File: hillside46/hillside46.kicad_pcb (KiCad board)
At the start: 2 copper layers, 142.5 x 99.9 mm, 92 parts, among them J2 TRRS, J3 Bat_Pos, J4 Bat_Neg, J5 XF2M-1215-1A, K1 SW_Key, K10 SW_Key, K11 SW_Key, K12 SW_Key, K13 SW_Key, K14 SW_Key, K15 SW_Key, K16 SW_Key, K17 SW_Key, K18 SW_Key, K19 SW_Rotary, K2 SW_Key, K20 SW_Rotary, K21 SW_Key, K22 SW_Key, K23 SW_Key, K3 SW_Key, K4 SW_Key, K5 SW_Key, K6 SW_Key, K7 SW_Key, K8 SW_Key, K9 SW_Key, SW1 SKQGAFE010, SW2 SW_Power, U1 NiceNano2_r, U2 SRV05-4

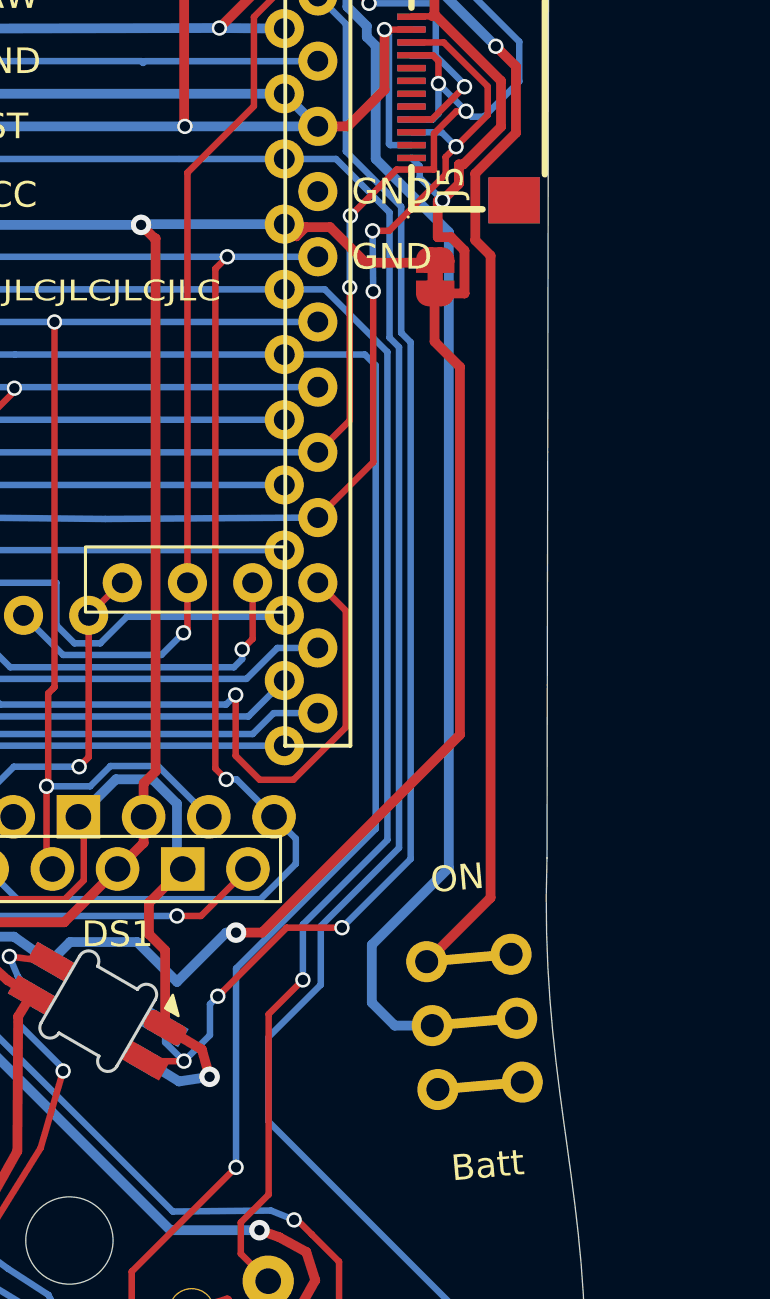
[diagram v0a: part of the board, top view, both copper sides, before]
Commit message: Adding mounting holes for the display cover
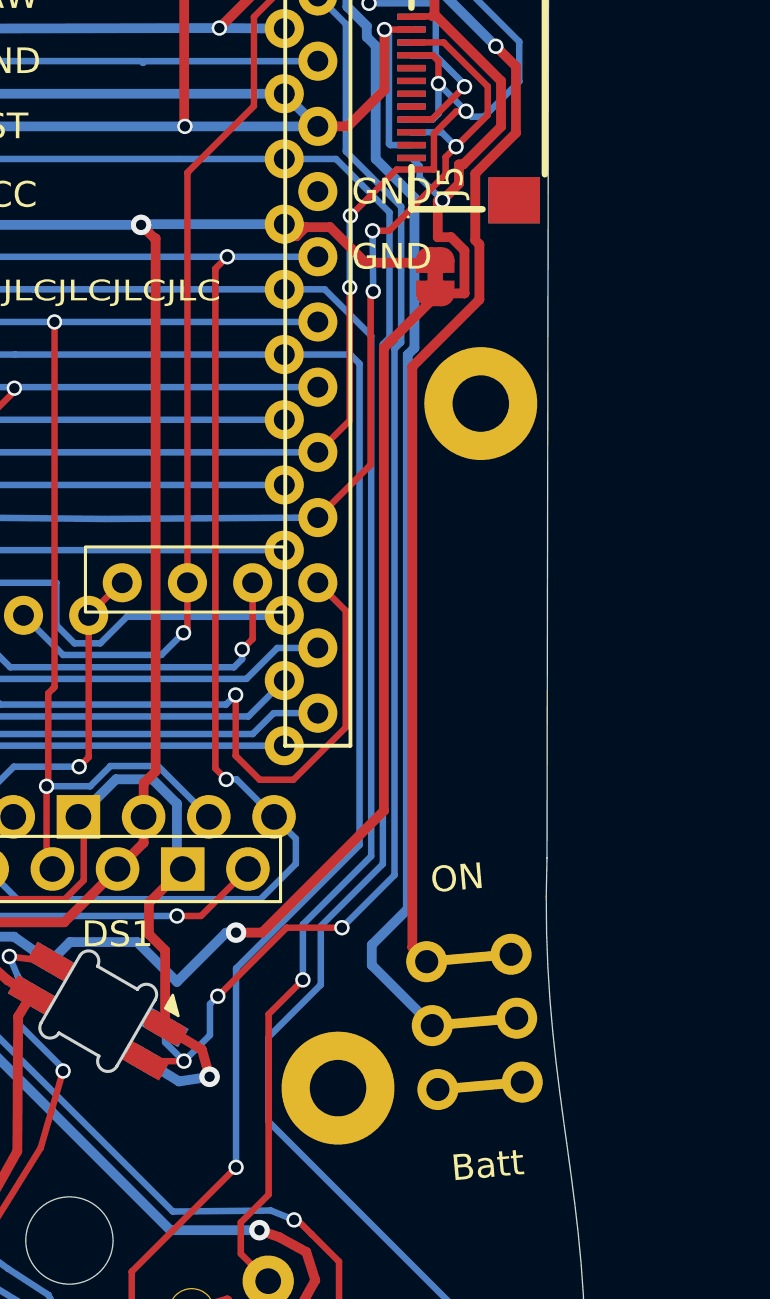
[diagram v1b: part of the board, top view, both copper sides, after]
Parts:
- added H32: MountHole, hillside:MountingHole_2.2mm_with_PCB_insert_rings, F.Cu at (206.9, 95.6)
- added H33: MountHole, hillside:MountingHole_2.2mm_with_PCB_insert_rings, F.Cu at (212.5, 68.9)
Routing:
- net bat+: track 61.0 -> 59.0 mm
- net enc_a: track 145.0 -> 144.1 mm
- net VCC_ACC: track 165.1 -> 164.3 mm
- net enc_b: track 141.6 -> 141.1 mm
